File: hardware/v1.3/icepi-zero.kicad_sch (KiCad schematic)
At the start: 29 parts, among them J1 Conn_02x20_Counter_Clockwise, SW1 SW_Push, SW2 SW_Push, U1 ECP5-CABGA256, Y1 SG-8018CG 50.000000MHz

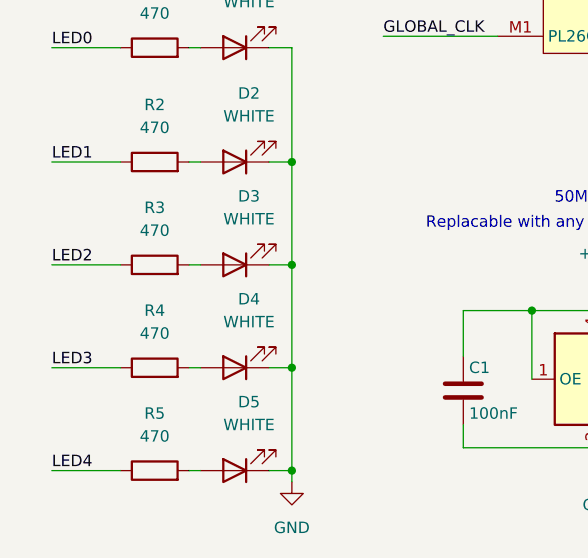
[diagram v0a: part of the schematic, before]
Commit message: Removed LEDs D3, D4, D5
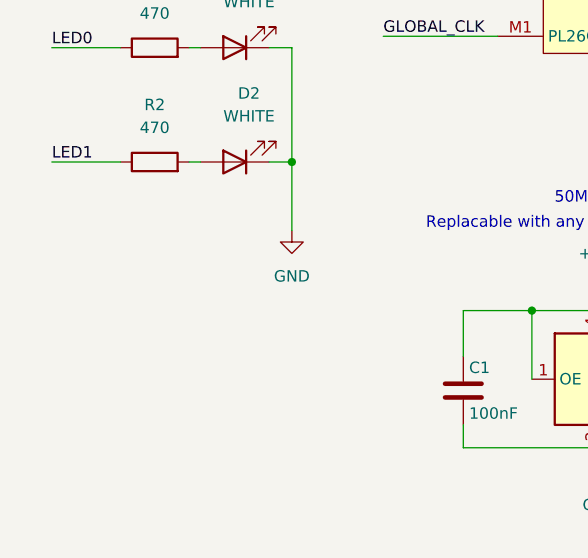
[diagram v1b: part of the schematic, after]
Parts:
- removed D3, D4, D5: WHITE, LED_SMD:LED_0603_1608Metric, symbol Device:LED
- removed R3, R4, R5: 470, Resistor_SMD:R_0402_1005Metric, symbol Device:R
